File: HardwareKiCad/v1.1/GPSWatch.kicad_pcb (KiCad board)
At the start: 2 copper layers, 41 x 42 mm, 58 parts, among them J1 USB_B_Micro, J2 Battery, J4 Micro_SD_Card_Det2, J5 Conn_01x04_Pin, SW1 EC05E1220401, SW2 SW_SPDT, SW3 SW_Push, SW4 SW_Push, SW5 SW_Push, U1 STM32F103C8Tx, U3 MCP73831-2-OT, U4 TPS2116DRL, U5 L96-M33, U6 BMA456, U7 AMS1117CS-3.3, Y1 ABM3-8.000MHZ-B4Y-T

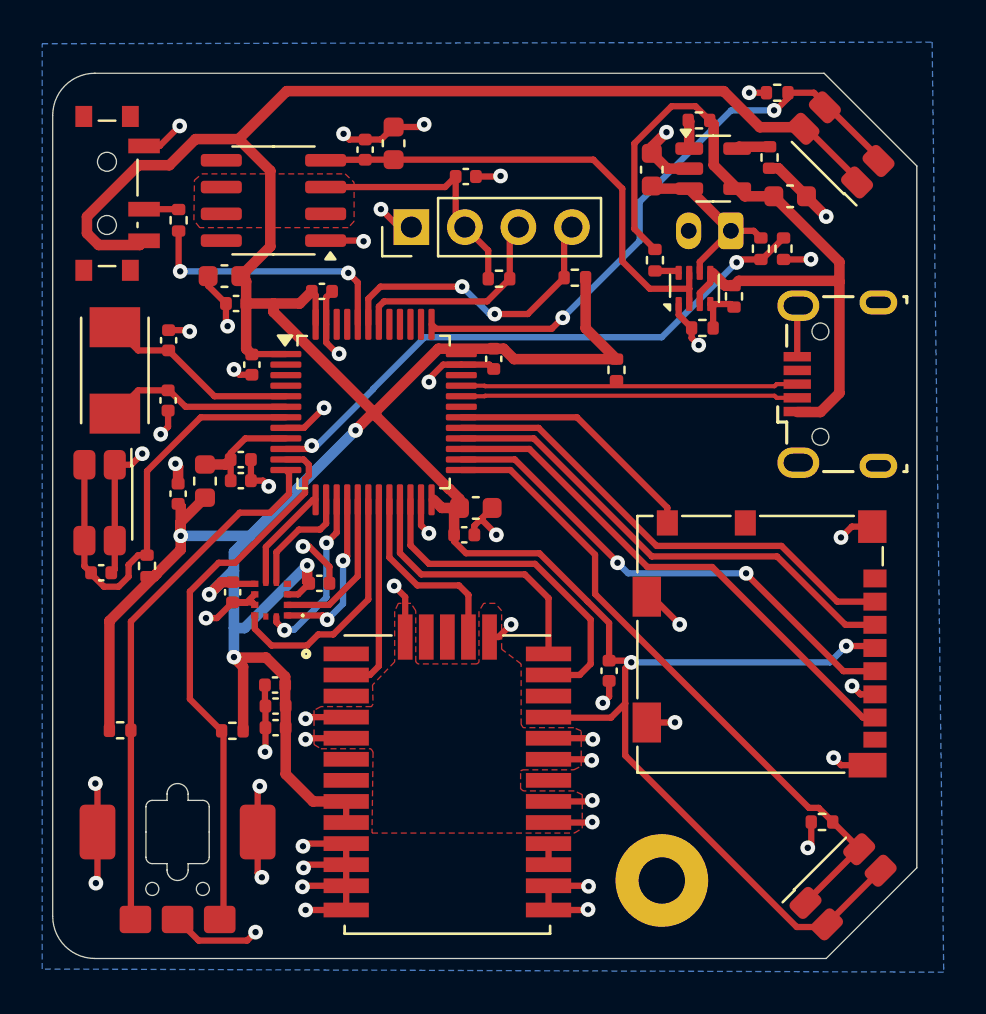
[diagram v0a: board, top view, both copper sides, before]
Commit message: Change MCP 73831 from SOIC 8 to SOT 223
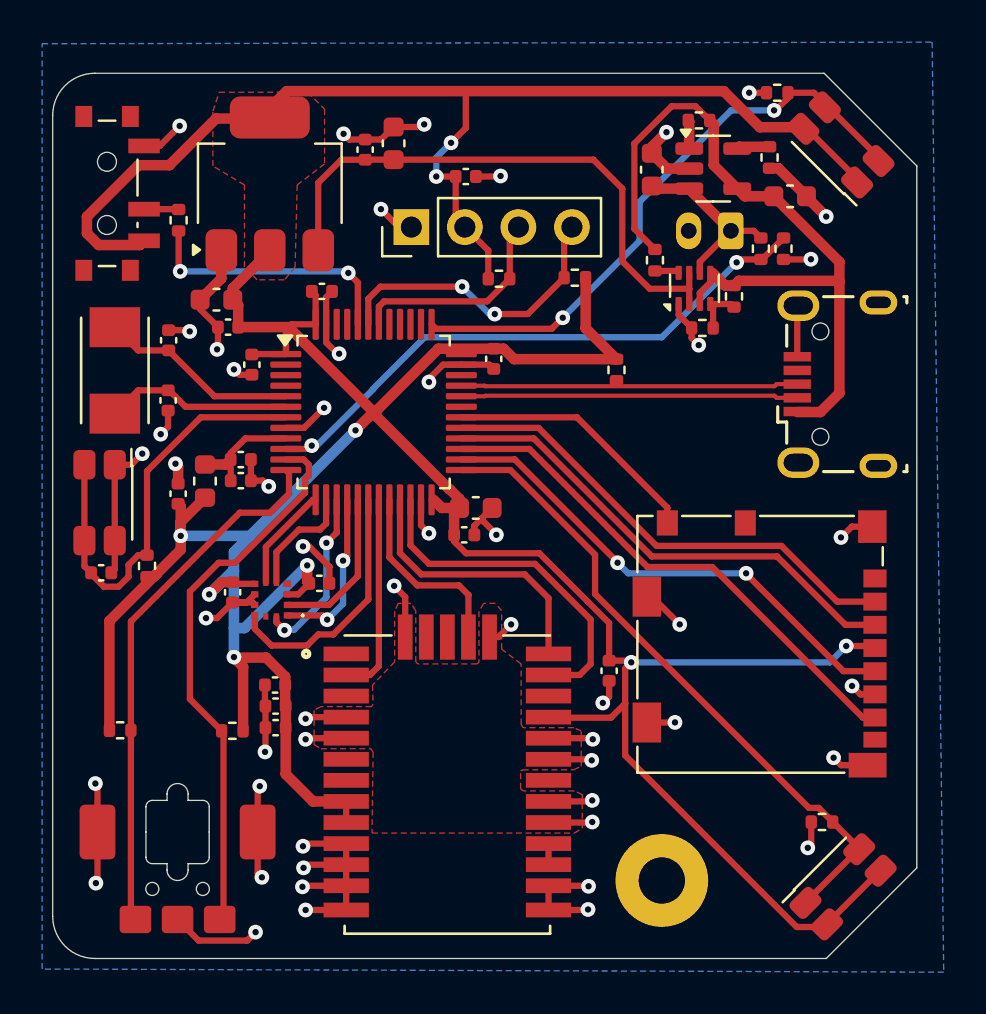
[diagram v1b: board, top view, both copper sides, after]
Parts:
- removed U7: AMS1117CS-3.3, Package_SO:SOIC-8_3.9x4.9mm_P1.27mm
- added U2: AMS1117-3.3, Package_TO_SOT_SMD:SOT-223-3_TabPin2, F.Cu at (144.8, 97.7)
- moved C13 1.18 mm to (142.3, 103.1)
- moved C14 1.18 mm to (142.8, 104.4)
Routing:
- net +3.3V: track 216.6 -> 209.1 mm, vias 7 -> 9
- net /VCC: track 23.3 -> 27.3 mm
- net GND: track 121.5 -> 122.4 mm, vias 52 -> 51
